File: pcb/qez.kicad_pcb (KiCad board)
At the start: 2 copper layers, 194.3 x 79 mm, 82 parts, among them U1 ATmega32U2-AU, U2 SRV05-4, X1 Crystal_GND24_Small

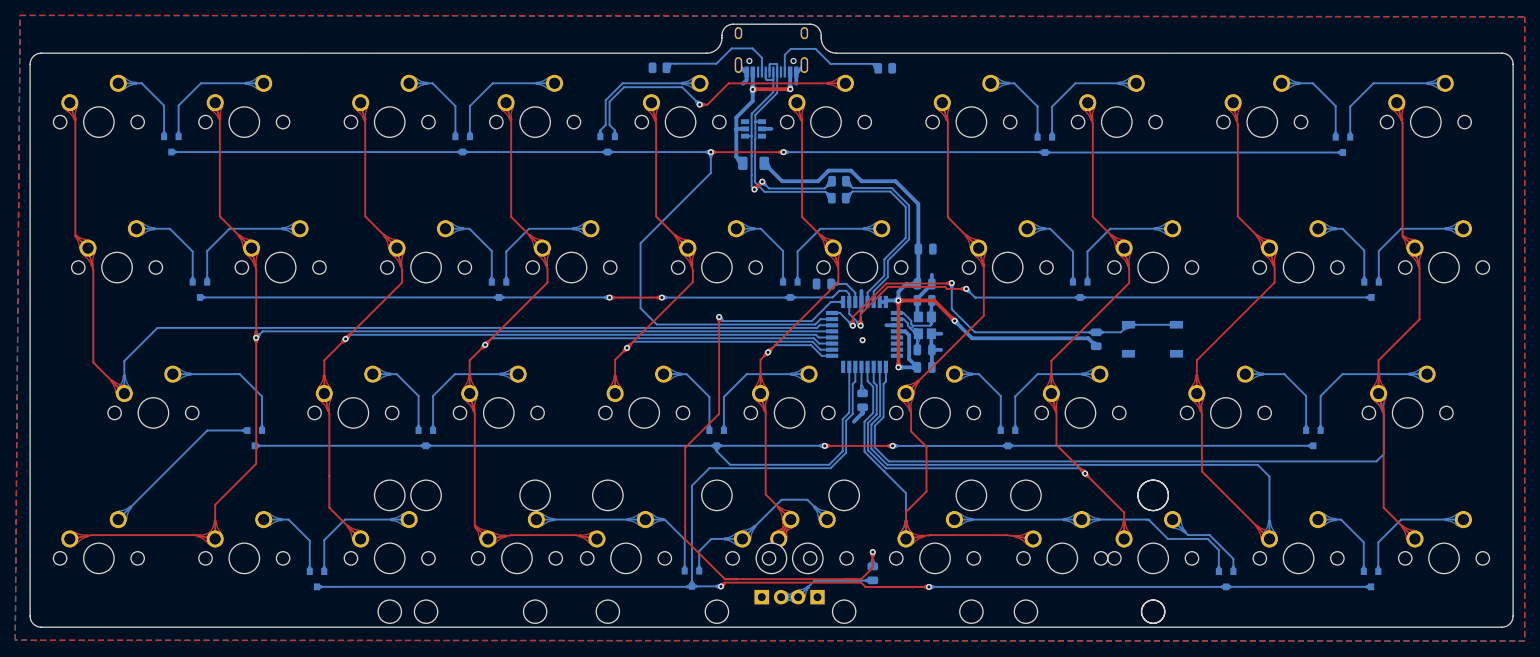
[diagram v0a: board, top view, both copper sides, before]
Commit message: Initial fork, P flipped
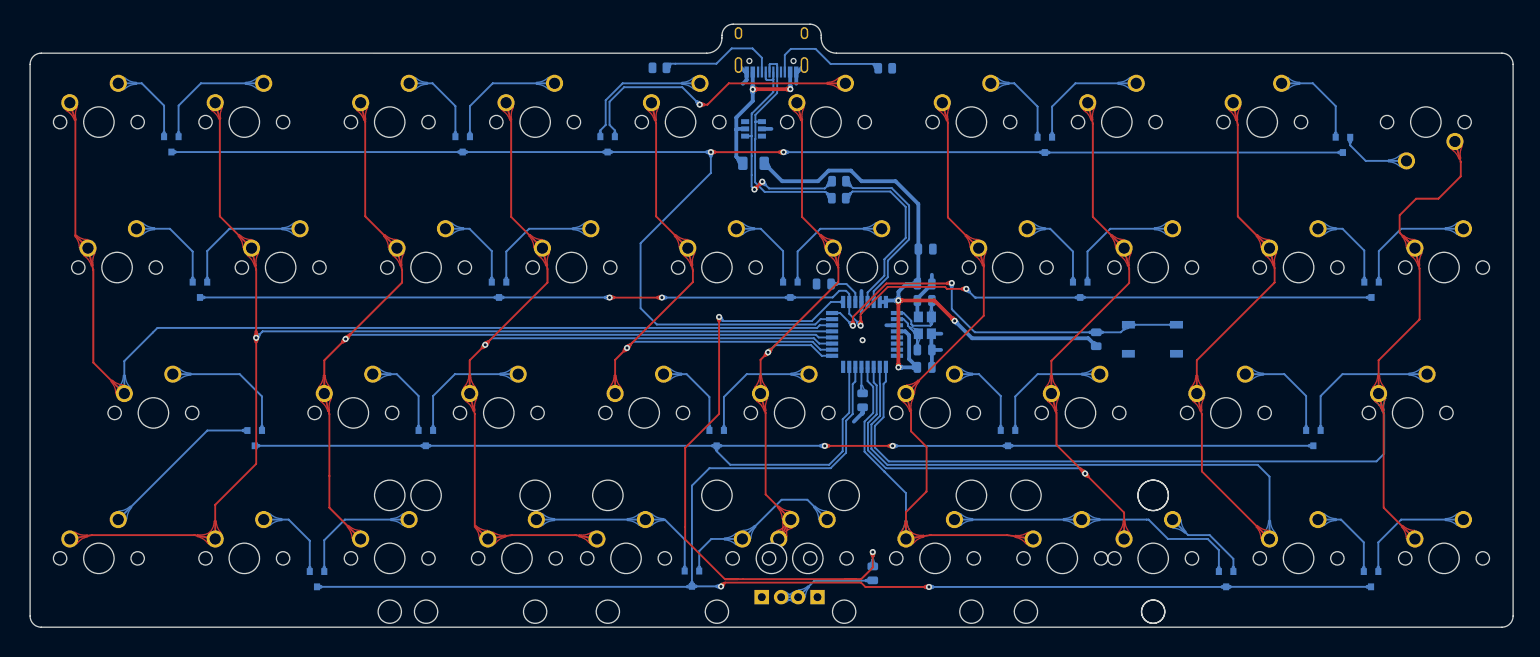
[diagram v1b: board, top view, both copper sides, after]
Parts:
- turned MX10 to 180 degrees
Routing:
- net Net-(D5-Pad2): track 30.1 -> 21.7 mm
- net col9: track 149.0 -> 151.4 mm
- removed copper zone on B.Cu, net GND
- removed copper zone on F.Cu, net GND
